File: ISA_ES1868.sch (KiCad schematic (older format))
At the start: 105 parts, among them J1 LINE IN, J10 Vol. Btns, J11 ISA BUS, J2 MIC, J3 Joystick/MIDI, J5 Wavetable, J7 SPKR OUT, J8 LINE OUT, U1 L78L05, U2 74LS138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

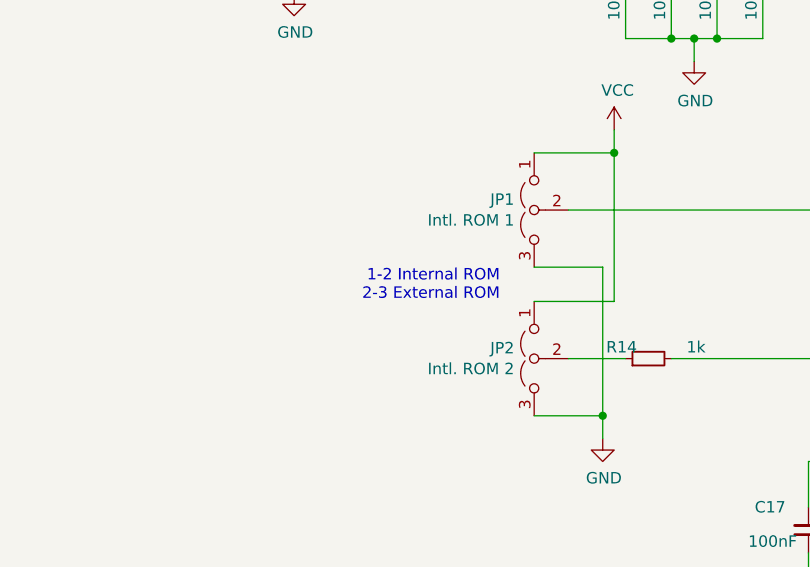
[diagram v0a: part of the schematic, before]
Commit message: Add description test
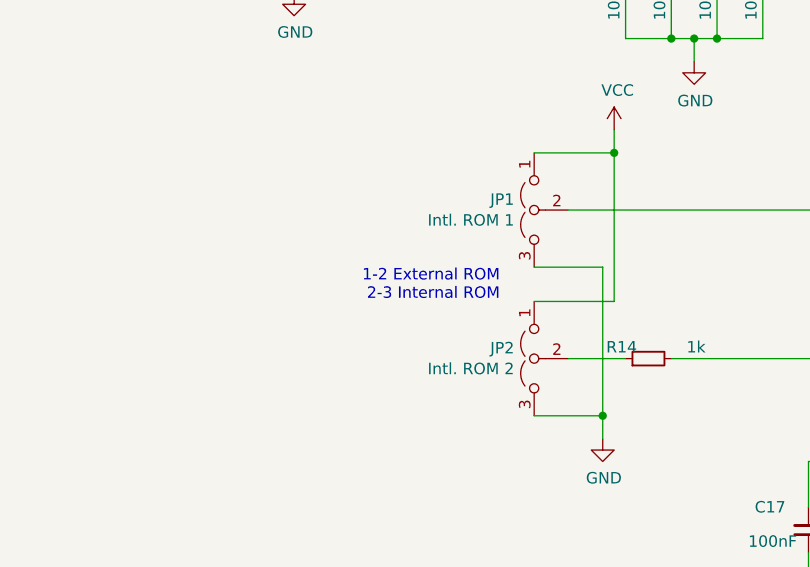
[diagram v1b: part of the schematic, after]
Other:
- note added: "1-2 External ROM\n2-3 Internal ROM"
- note removed: "1-2 Internal ROM\n2-3 External ROM"
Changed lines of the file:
@@
 Filtered_12V
 Text Notes 8500 11950 2    50   ~ 0
-1-2 Internal ROM\n2-3 External ROM
+1-2 External ROM\n2-3 Internal ROM
 $EndSCHEMATC

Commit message: Mark some unconnected pins as unconnected
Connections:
- net IOCHRDY: no longer names the net of J11.41 (IO_READY)
- net IRQ6: no longer names the net of J11.22 (IRQ6)
- no-connect marks 44 -> 46
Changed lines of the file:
@@
 $EndComp
 NoConn ~ 2300 8250
-Text Label 4400 7350 2    50   ~ 0
-IOCHRDY
-Wire Wire Line
-	3700 7350 4400 7350
 NoConn ~ 3700 7850
 NoConn ~ 3700 7750
@@
 Text Label 1600 8650 0    50   ~ 0
 IRQ5
-Text Label 1600 8550 0    50   ~ 0
-IRQ6
 Text Label 1600 8450 0    50   ~ 0
 IRQ7
@@
 	2300 8650 1600 8650
 Wire Wire Line
-	2300 8550 1600 8550
-Wire Wire Line
 	2300 8450 1600 8450
 Wire Wire Line
@@
 Text Notes 8500 11950 2    50   ~ 0
 1-2 External ROM\n2-3 Internal ROM
+NoConn ~ 3700 7350
+NoConn ~ 2300 8550
 $EndSCHEMATC

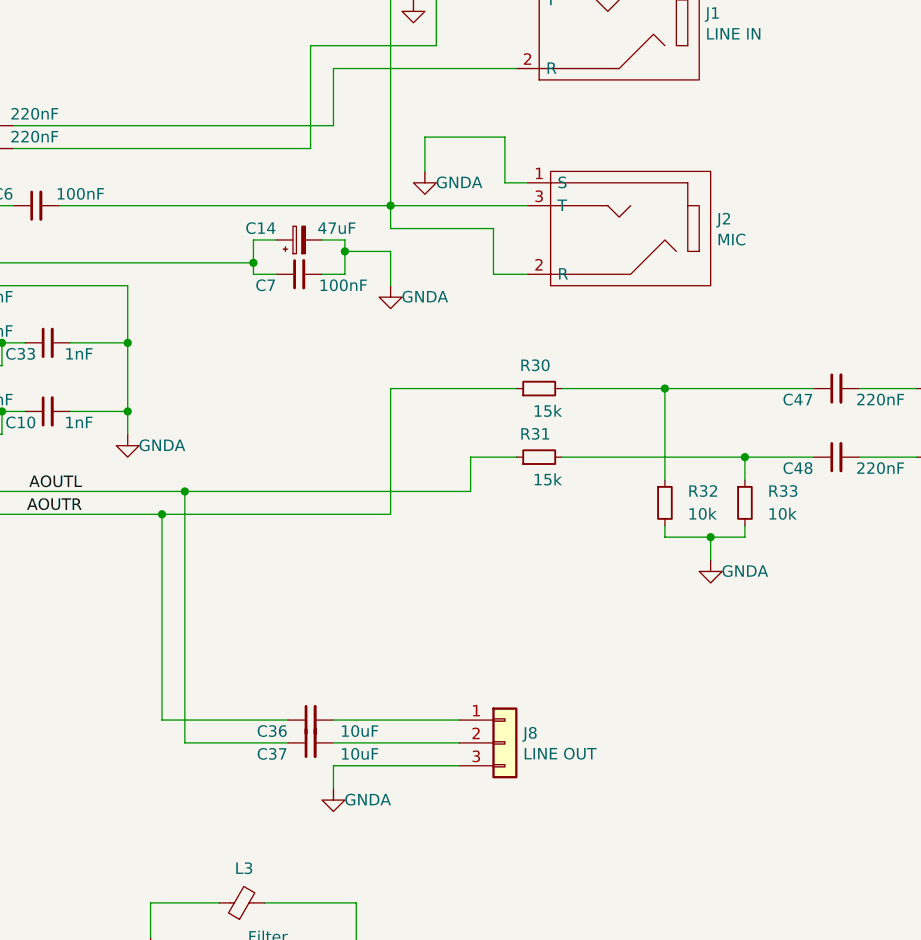
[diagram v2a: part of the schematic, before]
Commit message: Use put line out on jack
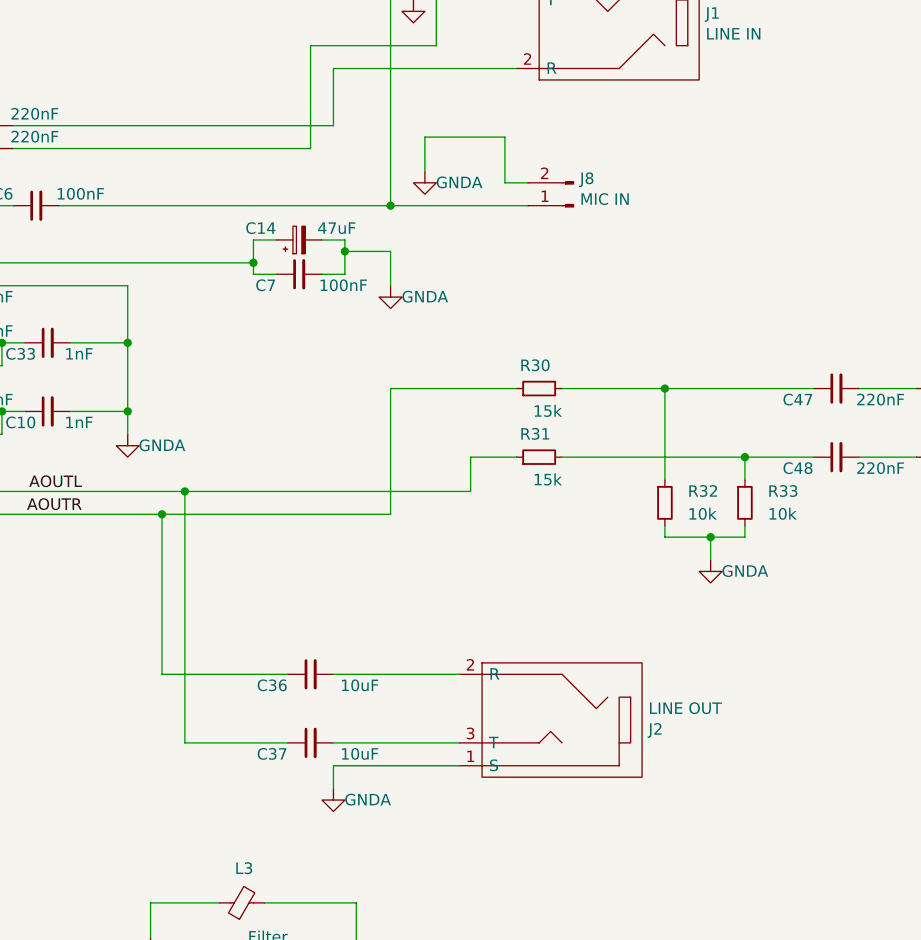
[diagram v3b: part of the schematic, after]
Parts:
- removed J8: LINE OUT, Connector_PinHeader_2.54mm:PinHeader_1x03_P2.54mm_Horizontal, symbol Connector_Generic:Conn_01x03
- added J8: MIC IN, Connector_PinHeader_2.54mm:PinHeader_1x02_P2.54mm_Horizontal, symbol Connector:Conn_01x02_Male
- J2: value MIC -> LINE OUT
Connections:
- net GNDA: now also J8.2 (Pin_2)
- net at C6.2, R2.2: now also J8.1 (Pin_1); no longer J2.2 (R), J2.3 (T)
- net at C36.2: now also J2.2 (R)
- net at C37.2: now also J2.3 (T)
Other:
- moved on the sheet: C36, J2
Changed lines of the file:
@@
 	12950 7400 14300 7400
 Wire Wire Line
-	14300 8500 14300 7400
-Wire Wire Line
-	14750 8500 14300 8500
-Wire Wire Line
 	12950 7500 14200 7500
 Wire Wire Line
-	14200 8400 14200 7500
-Wire Wire Line
-	14750 8400 14200 8400
-Wire Wire Line
-	14950 8500 15500 8500
-$Comp
-L Device:C_Small C37
-U 1 1 60B9D219
-P 14850 8500
-F 0 "C37" V 14900 8600 50  0000 L CNN
-F 1 "10uF" V 14900 8200 50  0000 L CNN
-F 2 "Capacitor_THT:C_Disc_D6.0mm_W2.5mm_P5.00mm" H 14850 8500 50  0001 C CNN
-F 3 "~" H 14850 8500 50  0001 C CNN
-	1    14850 8500
-	0    -1   1    0
-$EndComp
-$Comp
-L Device:C_Small C36
-U 1 1 60B9B492
-P 14850 8400
-F 0 "C36" V 14900 8500 50  0000 L CNN
-F 1 "10uF" V 14900 8100 50  0000 L CNN
-F 2 "Capacitor_THT:C_Disc_D6.0mm_W2.5mm_P5.00mm" H 14850 8400 50  0001 C CNN
-F 3 "~" H 14850 8400 50  0001 C CNN
-	1    14850 8400
-	0    -1   1    0
-$EndComp
+	14750 8200 14200 8200
 Wire Wire Line
 	14950 8600 14950 8700
@@
 	15100 4650 15200 4650
 Connection ~ 15200 6150
-Wire Wire Line
-	15200 6150 15200 6250
 Wire Wire Line
 	13750 6150 15200 6150
@@
 Wire Wire Line
 	14950 8600 15500 8600
-$Comp
-L my_components:JACK_TRS_3PINS J2
-U 1 1 62C8E737
-P 16250 6250
-F 0 "J2" H 15872 6209 50  0000 R CNN
-F 1 "MIC" H 15872 6300 50  0000 R CNN
-F 2 "My_Components:Conn_Audio_3.5mm_Stereo_SJ1-352XNG" H 15872 6346 50  0001 R CNN
-F 3 "" H 16400 6400 50  0000 C CNN
-	1    16250 6250
-	-1   0    0    1
-$EndComp
-Wire Wire Line
-	15650 6250 15650 6450
-Wire Wire Line
-	15650 6450 15800 6450
-Wire Wire Line
-	15200 6250 15650 6250
 Wire Wire Line
 	15200 6150 15800 6150
@@
 Text Label 13500 4650 0    50   ~ 0
 VDDA
-$Comp
-L Connector_Generic:Conn_01x03 J8
-U 1 1 633797AC
-P 15700 8500
-F 0 "J8" H 15780 8542 50  0000 L CNN
-F 1 "LINE OUT" H 15780 8451 50  0000 L CNN
-F 2 "Connector_PinHeader_2.54mm:PinHeader_1x03_P2.54mm_Horizontal" H 15700 8500 50  0001 C CNN
-F 3 "~" H 15700 8500 50  0001 C CNN
-	1    15700 8500
-	1    0    0    -1
-$EndComp
-Wire Wire Line
-	14950 8400 15500 8400
+Wire Wire Line
+	14950 8200 15500 8200
 Text Label 17550 4000 0    50   ~ 0
 Filtered_12V
@@
 NoConn ~ 3700 7350
 NoConn ~ 2300 8550
+$Comp
+L Connector:Conn_01x02_Male J8
+U 1 1 60A3C960
+P 16000 6150
+F 0 "J8" H 15972 6032 50  0000 R CNN
+F 1 "MIC IN" H 15972 6123 50  0000 R CNN
+F 2 "Connector_PinHeader_2.54mm:PinHeader_1x02_P2.54mm_Horizontal" H 16000 6150 50  0001 C CNN
+F 3 "~" H 16000 6150 50  0001 C CNN
+	1    16000 6150
+	-1   0    0    1
+$EndComp
+$Comp
+L my_components:JACK_TRS_3PINS J2
+U 1 1 62C8E737
+P 15950 8400
+F 0 "J2" H 15572 8359 50  0000 R CNN
+F 1 "LINE OUT" H 15572 8450 50  0000 R CNN
+F 2 "My_Components:Conn_Audio_3.5mm_Stereo_SJ1-352XNG" H 15572 8496 50  0001 R CNN
+F 3 "" H 16100 8550 50  0000 C CNN
+	1    15950 8400
+	-1   0    0    -1
+$EndComp
+Wire Wire Line
+	14300 8500 14300 7400
+$Comp
+L Device:C_Small C36
+U 1 1 60B9B492
+P 14850 8200
+F 0 "C36" V 14900 8300 50  0000 L CNN
+F 1 "10uF" V 14900 7900 50  0000 L CNN
+F 2 "Capacitor_THT:C_Disc_D6.0mm_W2.5mm_P5.00mm" H 14850 8200 50  0001 C CNN
+F 3 "~" H 14850 8200 50  0001 C CNN
+	1    14850 8200
+	0    -1   1    0
+$EndComp
+$Comp
+L Device:C_Small C37
+U 1 1 60B9D219
+P 14850 8500
+F 0 "C37" V 14900 8600 50  0000 L CNN
+F 1 "10uF" V 14900 8200 50  0000 L CNN
+F 2 "Capacitor_THT:C_Disc_D6.0mm_W2.5mm_P5.00mm" H 14850 8500 50  0001 C CNN
+F 3 "~" H 14850 8500 50  0001 C CNN
+	1    14850 8500
+	0    -1   1    0
+$EndComp
+Wire Wire Line
+	14950 8500 15500 8500
+Wire Wire Line
+	14750 8500 14300 8500
+Wire Wire Line
+	14200 8200 14200 7500
 $EndSCHEMATC

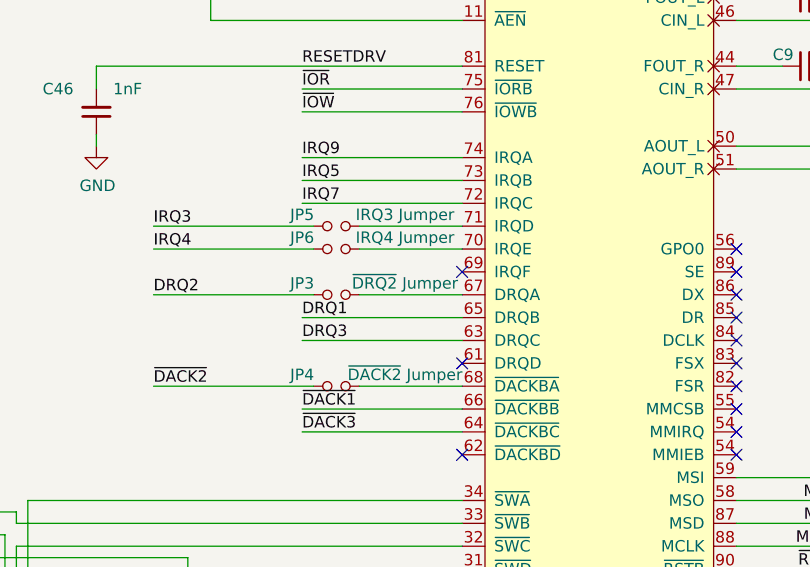
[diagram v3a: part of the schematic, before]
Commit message: Fixed silkscreen text
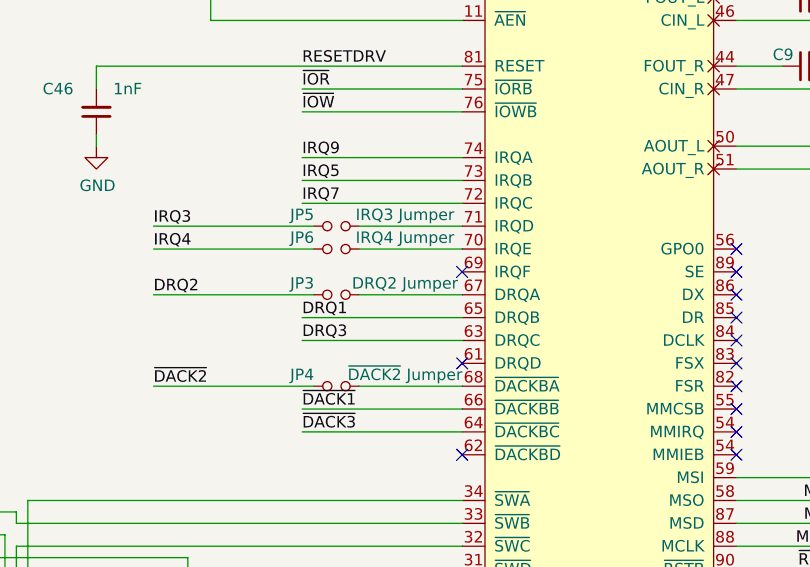
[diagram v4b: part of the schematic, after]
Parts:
- JP3: value ~DRQ2~ Jumper -> DRQ2 Jumper
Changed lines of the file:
@@
 P 11200 8050
 F 0 "JP3" H 11050 8100 50  0000 C CNN
-F 1 "~DRQ2~ Jumper" H 11500 8100 50  0000 C CNN
+F 1 "DRQ2 Jumper" H 11500 8100 50  0000 C CNN
 F 2 "Jumper:SolderJumper-2_P1.3mm_Open_RoundedPad1.0x1.5mm" H 11200 8050 50  0001 C CNN
 F 3 "~" H 11200 8050 50  0001 C CNN

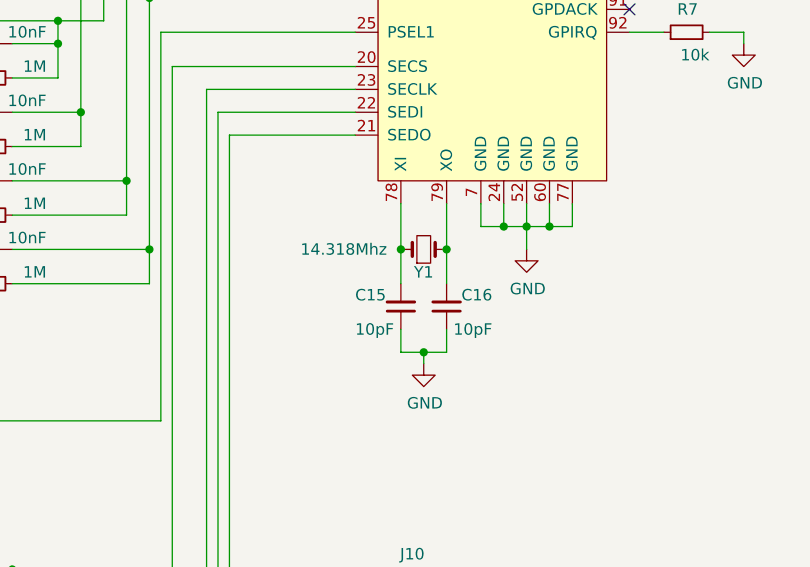
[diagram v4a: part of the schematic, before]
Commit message: Reorganized crystal on board and moved some traces
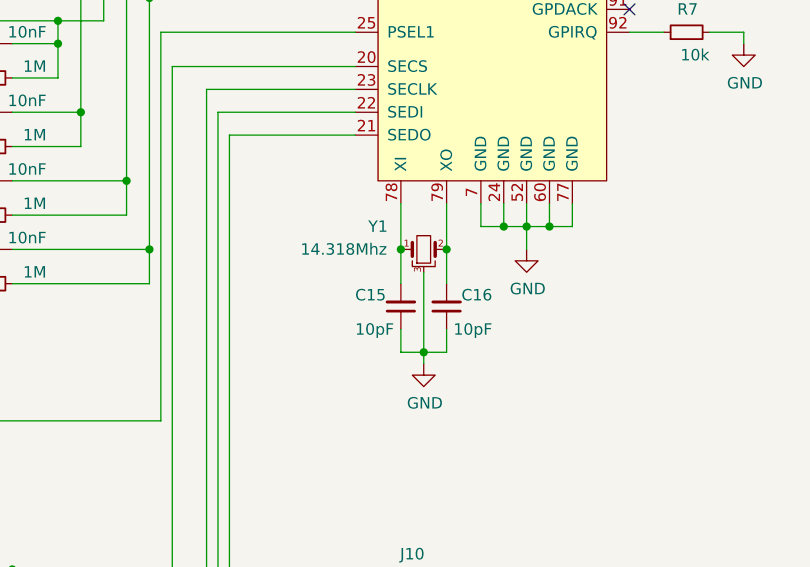
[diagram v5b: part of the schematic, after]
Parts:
- removed Y1: 14.318Mhz, Crystal:Crystal_HC49-4H_Vertical, symbol Device:Crystal_Small
- added Y1: 14.318Mhz, Crystal:Crystal_HC49-U_Horizontal_1EP_style2, symbol Device:Crystal_GND3_Small
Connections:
- net GND: now also Y1.3
- net at C15.2, U3.78 (XI): now also Y1.1
- net at C16.2, U3.79 (XO): now also Y1.2
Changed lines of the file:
@@
 Wire Wire Line
 	11950 11150 11950 11250
-Connection ~ 12150 10800
-Wire Wire Line
-	12150 10800 12150 10950
-Connection ~ 11950 10800
-Wire Wire Line
-	11950 10800 11950 10950
 $Comp
 L Device:C_Small C16
@@
 	1    11950 11050
 	1    0    0    1
-$EndComp
-Wire Wire Line
-	11950 10600 11950 10800
-Wire Wire Line
-	12150 10600 12150 10800
-$Comp
-L Device:Crystal_Small Y1
-U 1 1 60E0615D
-P 12050 10800
-F 0 "Y1" H 12050 10700 50  0000 C CNN
-F 1 "14.318Mhz" H 11700 10800 50  0000 C CNN
-F 2 "Crystal:Crystal_HC49-4H_Vertical" H 12050 10800 50  0001 C CNN
-F 3 "~" H 12050 10800 50  0001 C CNN
-	1    12050 10800
-	1    0    0    -1
 $EndComp
 Text Label 13400 8850 2    50   ~ 0
@@
 Wire Wire Line
 	14200 8200 14200 7500
+$Comp
+L Device:Crystal_GND3_Small Y1
+U 1 1 60AB9B18
+P 12050 10800
+F 0 "Y1" H 11850 10900 50  0000 C CNN
+F 1 "14.318Mhz" H 11700 10800 50  0000 C CNN
+F 2 "Crystal:Crystal_HC49-U_Horizontal_1EP_style2" H 12050 10800 50  0001 C CNN
+F 3 "~" H 12050 10800 50  0001 C CNN
+	1    12050 10800
+	1    0    0    -1
+$EndComp
+Wire Wire Line
+	11950 10600 11950 10800
+Wire Wire Line
+	12150 10600 12150 10800
+Connection ~ 11950 10800
+Wire Wire Line
+	11950 10800 11950 10950
+Connection ~ 12150 10800
+Wire Wire Line
+	12150 10800 12150 10950
+Wire Wire Line
+	12050 10900 12050 11250
 $EndSCHEMATC

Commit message: Add SB DB15 connector
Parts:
- J3: footprint Connector_Dsub:DSUB-15_Female_Horizontal_P2.77x2.84mm_EdgePinOffset4.94mm_Housed_MountingHolesOffset7.48mm -> Custom_Connectors:SB_DB15_152-3415
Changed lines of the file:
@@
 F 0 "J3" H 6655 9409 50  0000 L CNN
 F 1 "Joystick/MIDI" H 6655 9500 50  0000 L CNN
-F 2 "Connector_Dsub:DSUB-15_Female_Horizontal_P2.77x2.84mm_EdgePinOffset4.94mm_Housed_MountingHolesOffset7.48mm" H 6500 9500 50  0001 C CNN
+F 2 "Custom_Connectors:SB_DB15_152-3415" H 6500 9500 50  0001 C CNN
 F 3 " ~" H 6500 9500 50  0001 C CNN
 	1    6500 9500

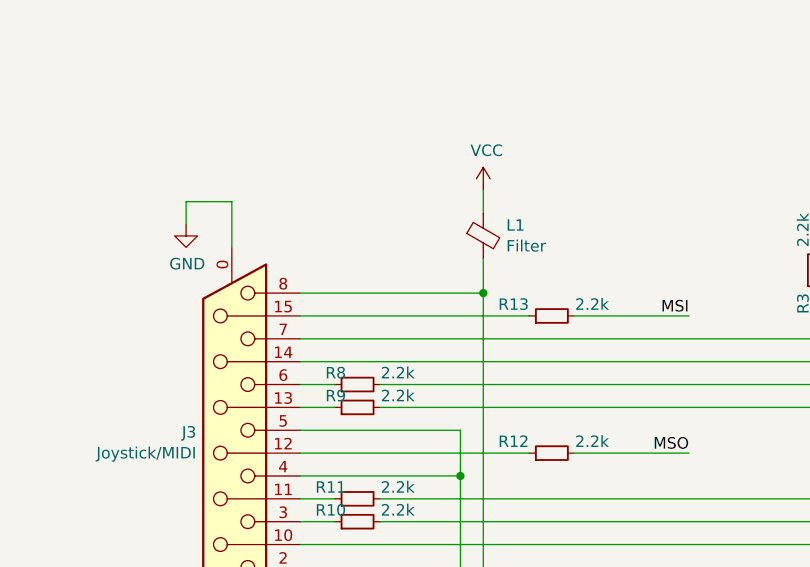
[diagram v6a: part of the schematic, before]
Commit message: Rerouted and resized some traces
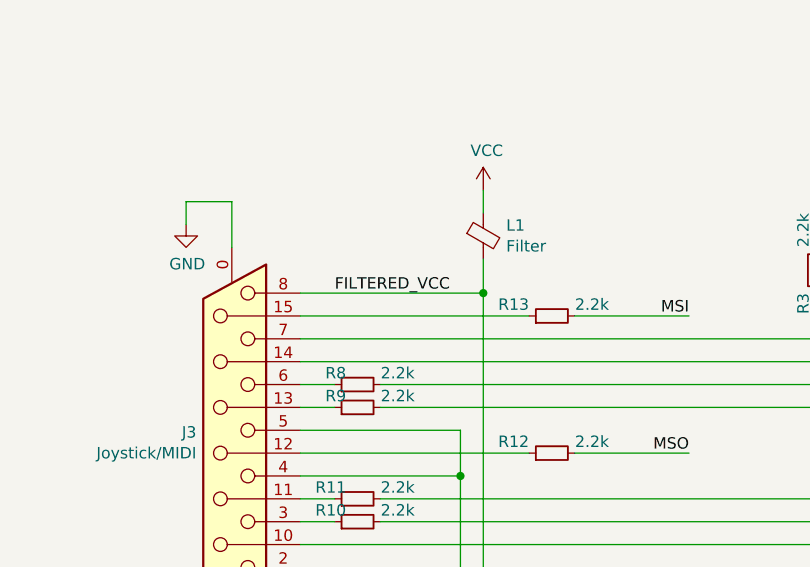
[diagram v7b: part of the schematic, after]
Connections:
- net FILTERED_VCC: now reaches C22.2, J3.1, J3.8, J3.9 (P9), L1.2
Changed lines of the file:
@@
 Wire Wire Line
 	12050 10900 12050 11250
+Text Label 6950 8800 0    50   ~ 0
+FILTERED_VCC
 $EndSCHEMATC
